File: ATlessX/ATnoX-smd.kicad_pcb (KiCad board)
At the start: 2 copper layers, 31 parts, among them J1 EXT_PWR_SW, J2 ATX, J3 P8, J4 P9, SW1 Power, U1 74LS74, U2 74LS14, U3 L7905

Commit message: Update PCB
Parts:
- moved J3 86.2 mm to (209.6, 129.5)
- moved J4 86.2 mm to (226.1, 129.5)
- moved C2 81.2 mm to (231.2, 115.0)
- moved C3 81.2 mm to (220.6, 113.7)
- moved R3 81.2 mm to (245.8, 109.2)
- moved R2 81.2 mm to (212.0, 117.2)
- moved R4 81.2 mm to (248.4, 103.9)
- moved R8 81.2 mm to (218.0, 117.2)
- moved C4 81.2 mm to (223.9, 117.0)
- moved D3 81.2 mm to (251.6, 107.3)
- moved D4 81.2 mm to (254.2, 101.6)
- moved D6 81.2 mm to (245.1, 112.5)
- moved D7 81.2 mm to (239.2, 116.1)
- moved R1 81.2 mm to (254.4, 98.3)
- moved R5 81.2 mm to (239.3, 112.7)
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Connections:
- D5 pad 2: (no net) -> /+12V
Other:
- board outline added: 80 x 47 mm

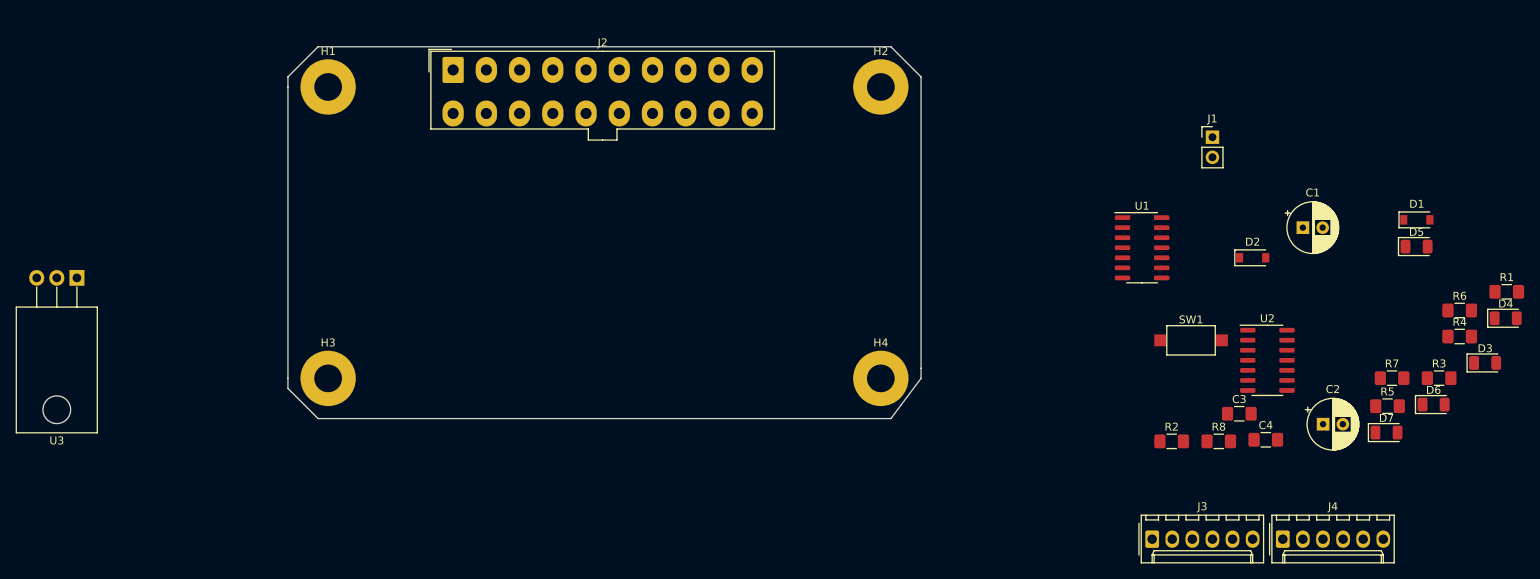
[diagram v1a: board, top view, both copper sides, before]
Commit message: Add SMD variant
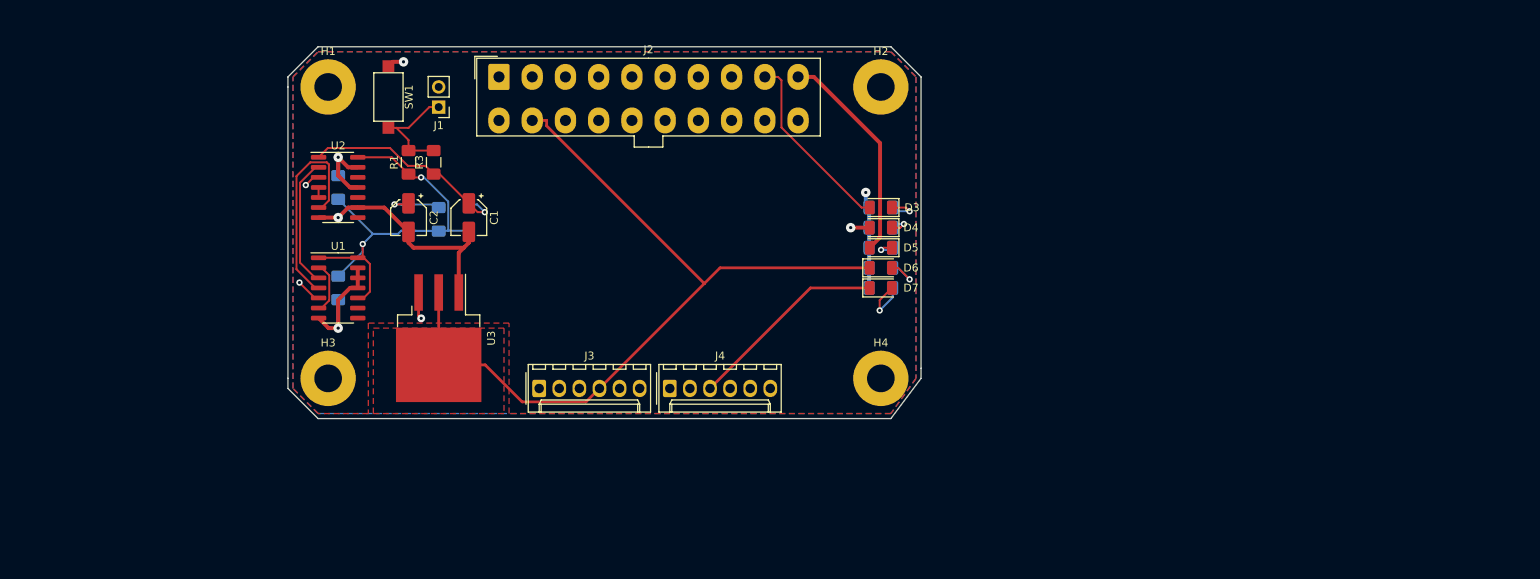
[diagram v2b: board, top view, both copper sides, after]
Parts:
- C1, C2: footprint Capacitor_THT:CP_Radial_D6.3mm_P2.50mm -> Capacitor_SMD:CP_Elec_4x5.3
- C3, C4, D1, D2, R2, R4, R5, R6, R7, R8: moved to B.Cu
- U3: footprint Package_TO_SOT_THT:TO-220-3_Horizontal_TabDown -> Package_TO_SOT_SMD:TO-263-3_TabPin2
- moved R1 139.8 mm to (115.6, 81.9), turned to 90 degrees
- moved R3 130.0 mm to (118.7, 81.9), turned to 90 degrees
- moved D1 119.8 mm to (123.2, 88.9), turned to 90 degrees
- moved U2 119.5 mm to (106.7, 85.1)
- moved C4 118.8 mm to (106.7, 97.8), turned to 270 degrees
- moved C2 118.5 mm to (115.6, 88.9), turned to 270 degrees
- moved C3 117.4 mm to (106.7, 85.1), turned to 90 degrees
- moved D2 106.8 mm to (115.6, 88.9), turned to 90 degrees
- moved SW1 106.0 mm to (113.0, 73.7), turned to 270 degrees
- moved C1 105.4 mm to (123.2, 88.9), turned to 270 degrees
- moved U1 101.7 mm to (106.7, 97.8)
- moved J1 97.9 mm to (119.4, 74.9), turned to 180 degrees
- moved R2 96.8 mm to (119.4, 89.1), turned to 90 degrees
- moved D4 79.8 mm to (175.3, 90.2), turned to 180 degrees
- moved J3 79.8 mm to (132.1, 110.5)
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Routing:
- net GND: track 0.00 -> 321.4 mm, vias 0 -> 5
- net /5VSB: track 0.00 -> 133.3 mm, vias 0 -> 2
- net VCC: track 0.00 -> 121.5 mm, vias 0 -> 1
- net /-12V: track 0.00 -> 103.3 mm
- net /+12V: track 0.00 -> 79.6 mm
- net /-5V: track 0.00 -> 70.4 mm, vias 0 -> 1
- net /PWR_OK: track 0.00 -> 50.4 mm
- net /~PS_ON: track 0.00 -> 49.8 mm, vias 0 -> 1
- net Net-(C1-Pad1): track 0.00 -> 27.3 mm, vias 0 -> 1
- net Net-(U1-Pad4): track 0.00 -> 26.7 mm
- net Net-(C2-Pad1): track 0.00 -> 21.8 mm, vias 0 -> 2
- net Net-(U1-Pad3): track 0.00 -> 16.4 mm
- net /PWR_SW: track 0.00 -> 14.1 mm
- net Net-(D7-Pad2): track 0.00 -> 7.01 mm, vias 0 -> 1
- net Net-(U1-Pad2): track 0.00 -> 6.65 mm
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- added copper zone on F.Cu, net /-12V
- added copper zone on B.Cu, net GND
- added copper zone on F.Cu, net GND
- added copper zone on In1.Cu, net GND
- added copper zone on In2.Cu, net VCC
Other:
- copper layers 2 -> 4

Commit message: Better ATnoX PCB
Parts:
- renumbered J3 to P8, J4 to P9
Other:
- board text added: "+12V"
- board text added: "+5V"
- board text added: "-12V"
- board text added: "-5V"
- board text added: "5VSB"
- board text added: "74HC14"
- board text added: "74HC74"
- board text added: "7905"
- board text added: "AT Power Connector"
- board text added: "ATX Power Connector"
- board text added: "ATnoX"
- board text added: "Design by"
- board text added: "Power Button"
- board text added: "SMD - Proto"
- board text added: "tabaglio@posteo.net"
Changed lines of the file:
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@@
   (general
     (thickness 1.6)
-    (drawings 11)
+    (drawings 26)
     (tracks 283)
     (zones 0)
@@
     (tags "D2PAK DDPAK TO-263 D2PAK-3 TO-263-3 SOT-404")
     (attr smd)
-    (fp_text reference U3 (at 0 -6.65 90) (layer F.SilkS)
+    (fp_text reference U3 (at -3.81 -5.08) (layer F.SilkS)
       (effects (font (size 1 1) (thickness 0.15)))
     )
@@
     (tags "SPST button tactile switch")
     (attr smd)
-    (fp_text reference SW1 (at 0 -2.6 90) (layer F.SilkS)
+    (fp_text reference SW1 (at 0 0 90) (layer F.SilkS)
       (effects (font (size 1 1) (thickness 0.15)))
     )
@@
     (tags "resistor handsolder")
     (attr smd)
-    (fp_text reference R6 (at 0 1.82) (layer B.SilkS)
+    (fp_text reference R6 (at -3.81 0) (layer B.SilkS)
       (effects (font (size 1 1) (thickness 0.15)) (justify mirror))
     )
@@
     (descr "Molex KK-254 Interconnect System, old/engineering part number: AE-6410-06A example for new part number: 22-27-2061, 6 Pins (http://www.molex.com/pdm_docs/sd/022272021_sd.pdf), generated with kicad-footprint-generator")
     (tags "connector Molex KK-254 side entry")
-    (fp_text reference J4 (at 6.35 -4.12) (layer F.SilkS)
+    (fp_text reference P9 (at 6.35 -4.12) (layer F.SilkS)
       (effects (font (size 1 1) (thickness 0.15)))
     )
@@
     (descr "Molex KK-254 Interconnect System, old/engineering part number: AE-6410-06A example for new part number: 22-27-2061, 6 Pins (http://www.molex.com/pdm_docs/sd/022272021_sd.pdf), generated with kicad-footprint-generator")
     (tags "connector Molex KK-254 side entry")
-    (fp_text reference J3 (at 6.35 -4.12) (layer F.SilkS)
+    (fp_text reference P8 (at 6.35 -4.12) (layer F.SilkS)
       (effects (font (size 1 1) (thickness 0.15)))
     )
@@
     (descr "Through hole straight pin header, 1x02, 2.54mm pitch, single row")
     (tags "Through hole pin header THT 1x02 2.54mm single row")
-    (fp_text reference J1 (at 0 -2.33) (layer F.SilkS)
+    (fp_text reference J1 (at -2.54 1.27 90) (layer F.SilkS)
       (effects (font (size 1 1) (thickness 0.15)))
     )
@@
     )
   )
+  (gr_text tabaglio@posteo.net (at 102.87 86.36 270) (layer B.SilkS)
+    (effects (font (size 1 1) (thickness 0.15) italic) (justify mirror))
+  )
+  (gr_text "Design by" (at 102.87 99.06 270) (layer B.SilkS)
+    (effects (font (size 1 1) (thickness 0.25)) (justify mirror))
+  )
+  (gr_text "SMD - Proto" (at 137.16 97.79) (layer F.SilkS)
+    (effects (font (size 1 1) (thickness 0.15) italic))
+  )
+  (gr_text ATnoX (at 146.05 93.98) (layer F.SilkS)
+    (effects (font (size 6 6) (thickness 0.5) italic))
+  )
+  (gr_text 7905 (at 113.03 100.33) (layer F.SilkS)
+    (effects (font (size 1 1) (thickness 0.15)))
+  )
+  (gr_text 74HC74 (at 106.68 97.79 90) (layer F.SilkS)
+    (effects (font (size 1 1) (thickness 0.15)))
+  )
+  (gr_text 74HC14 (at 106.68 85.09 90) (layer F.SilkS)
+    (effects (font (size 1 1) (thickness 0.15)))
+  )
+  (gr_text "Power Button" (at 116.84 73.66 90) (layer F.SilkS)
+    (effects (font (size 1 1) (thickness 0.15)))
+  )
+  (gr_text -5V (at 168.91 97.79) (layer F.SilkS)
+    (effects (font (size 1 1) (thickness 0.15)) (justify left))
+  )
+  (gr_text -12V (at 168.91 95.25) (layer F.SilkS)
+    (effects (font (size 1 1) (thickness 0.15)) (justify left))
+  )
+  (gr_text +12V (at 168.91 92.71) (layer F.SilkS)
+    (effects (font (size 1 1) (thickness 0.15)) (justify left))
+  )
+  (gr_text +5V (at 168.91 90.17) (layer F.SilkS)
+    (effects (font (size 1 1) (thickness 0.15)) (justify left))
+  )
+  (gr_text 5VSB (at 168.91 87.63) (layer F.SilkS)
+    (effects (font (size 1 1) (thickness 0.15)) (justify left))
+  )
+  (gr_text "ATX Power Connector" (at 146.05 81.28) (layer F.SilkS)
+    (effects (font (size 1 1) (thickness 0.15)))
+  )
+  (gr_text "AT  Power Connector" (at 146.05 104.14) (layer F.SilkS)
+    (effects (font (size 1 1) (thickness 0.15)))
+  )
   (gr_line (start 176.53 114.3) (end 180.34 109.22) (layer Edge.Cuts) (width 0.1))

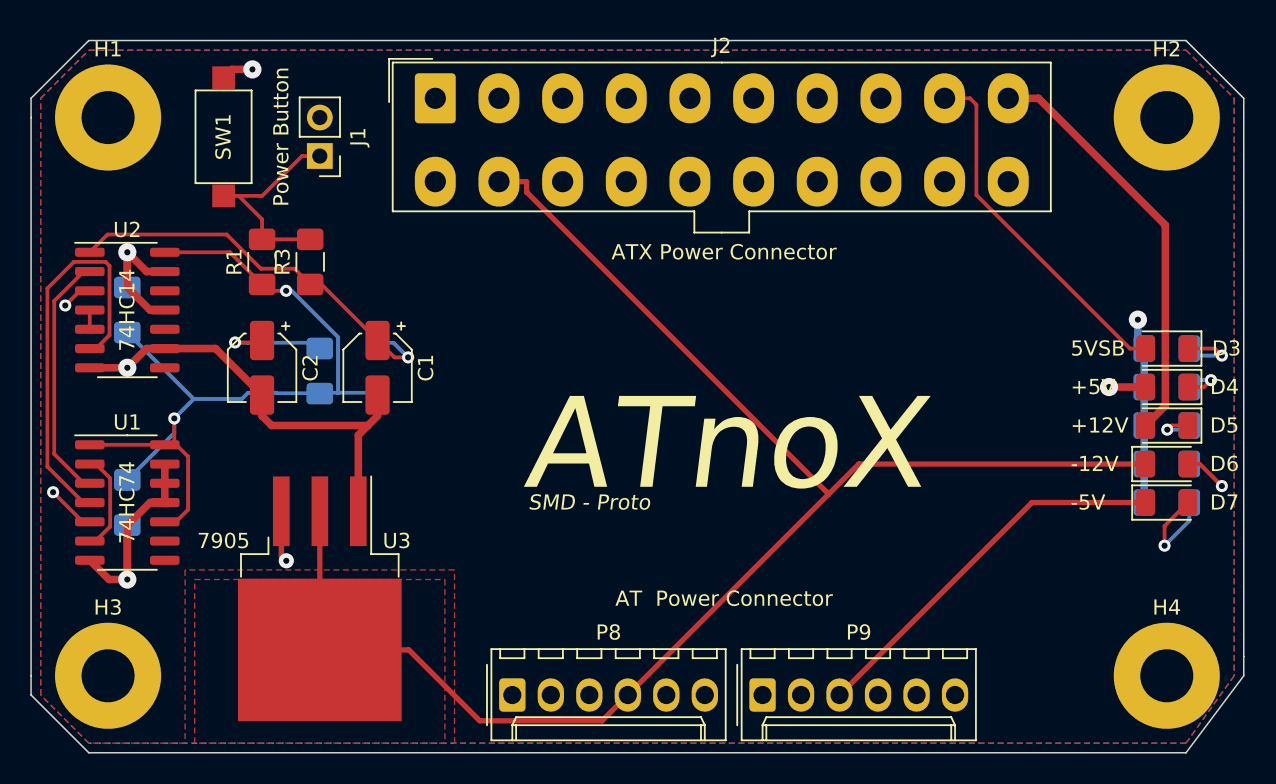
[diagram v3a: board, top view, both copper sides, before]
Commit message: Turned the SMD version into a 4layer board
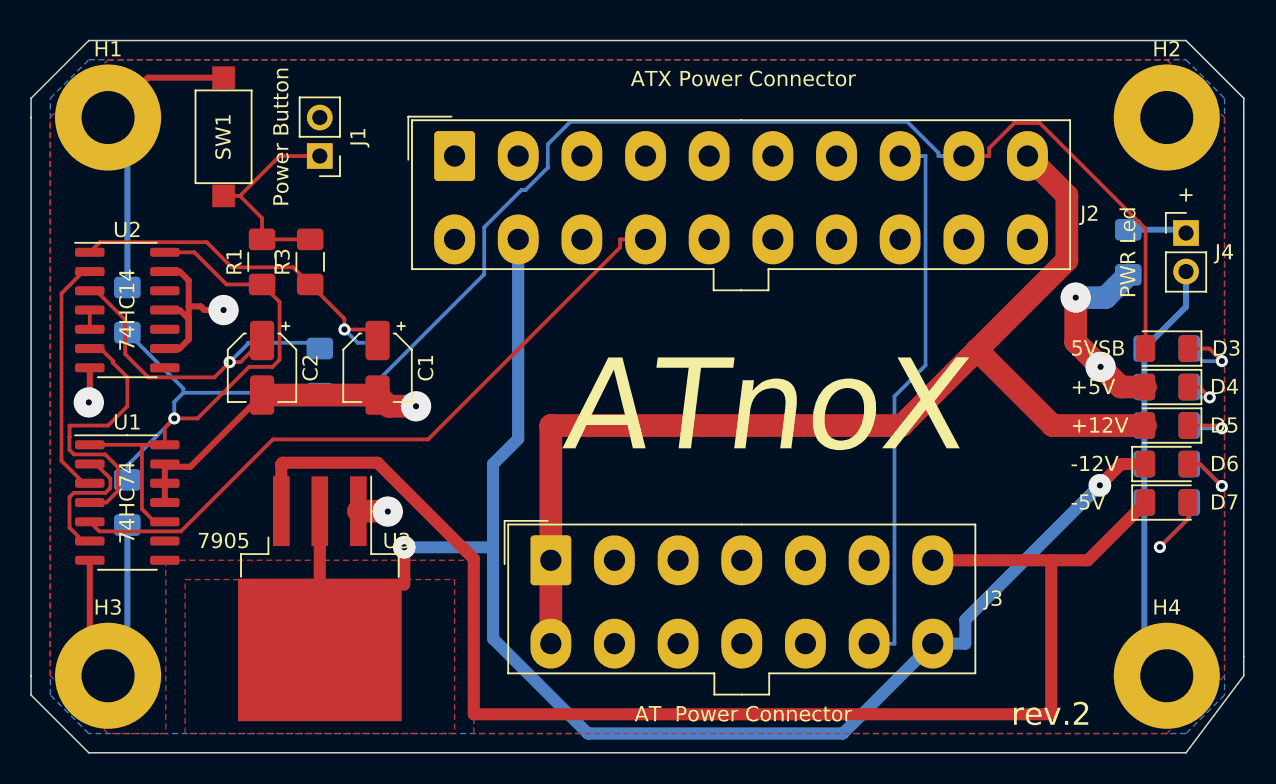
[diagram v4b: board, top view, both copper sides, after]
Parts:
- removed P8: P8, Connector_Molex:Molex_KK-254_AE-6410-06A_1x06_P2.54mm_Vertical
- removed P9: P9, Connector_Molex:Molex_KK-254_AE-6410-06A_1x06_P2.54mm_Vertical
- added J3: AT, Connector_Molex:Molex_Mini-Fit_Jr_5566-14A_2x07_P4.20mm_Vertical, F.Cu at (134.6, 101.6)
- added J4: PWR_LED, Connector_PinHeader_2.54mm:PinHeader_1x02_P2.54mm_Vertical, F.Cu at (176.5, 80.0)
- added R9: 1K, Resistor_SMD:R_1206_3216Metric_Pad1.42x1.75mm_HandSolder, B.Cu at (172.7, 81.3)
- moved J2 4.02 mm to (128.3, 74.9)
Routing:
- net GND: track 321.4 -> 389.8 mm, vias 5 -> 4
- net /-5V: track 70.4 -> 92.6 mm, vias 1 -> 0
- net /PWR_OK: track 50.4 -> 36.4 mm
- net Net-(U1-Pad4): track 26.7 -> 18.6 mm
- net VCC: track 121.5 -> 115.1 mm, vias 1 -> 2
- net /+12V: track 79.6 -> 74.1 mm
- net /~PS_ON: track 49.8 -> 45.2 mm, vias 1 -> 0
- net Net-(J4-Pad1): track 0.00 -> 3.90 mm
- net Net-(U1-Pad2): track 6.65 -> 9.03 mm
- net Net-(C1-Pad1): track 27.3 -> 24.9 mm
- net Net-(D5-Pad1): track 3.05 -> 4.53 mm
- net /-12V: track 103.3 -> 101.8 mm, vias 0 -> 2
- net /5VSB: track 133.3 -> 134.5 mm, vias 2 -> 1
- net Net-(C2-Pad1): track 21.8 -> 22.7 mm, vias 2 -> 1
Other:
- net class HiPower: trace_width 0.5 -> 1.5; via_dia 1.2 -> 2
- net class Power: clearance 0.3 -> 0.4; trace_width 0.35 -> 0.8; via_dia 1 -> 1.5
- board text added: "+"
- board text added: "PWR Led"
- board text added: "rev.2"
- board text removed: "SMD - Proto"

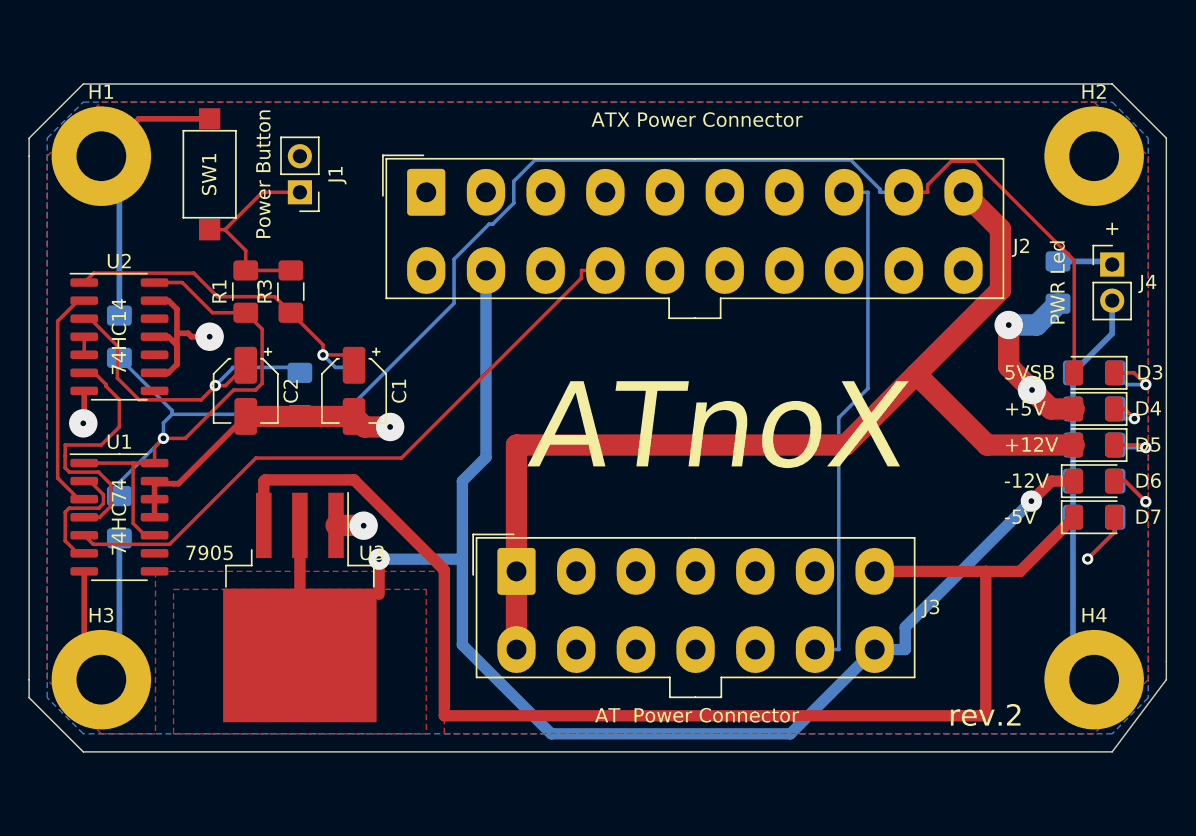
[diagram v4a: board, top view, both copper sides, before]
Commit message: Add rev. 2.5 of SMD variant
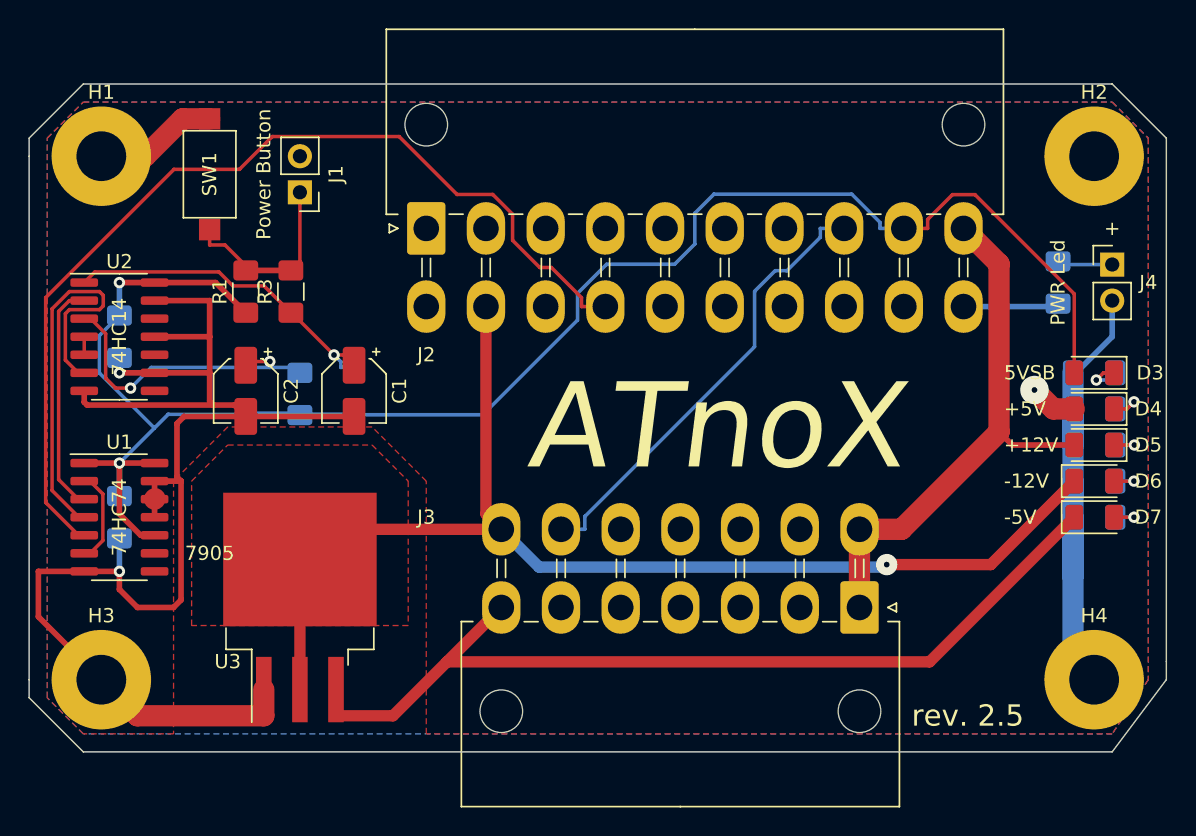
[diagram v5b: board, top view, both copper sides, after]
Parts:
- J2: footprint Connector_Molex:Molex_Mini-Fit_Jr_5566-20A_2x10_P4.20mm_Vertical -> Connector_Molex:Molex_Mini-Fit_Jr_5569-20A2_2x10_P4.20mm_Horizontal
- J3: footprint Connector_Molex:Molex_Mini-Fit_Jr_5566-14A_2x07_P4.20mm_Vertical -> Connector_Molex:Molex_Mini-Fit_Jr_5569-14A2_2x07_P4.20mm_Horizontal
- moved J3 24.3 mm to (158.8, 104.1), turned to 180 degrees
- moved J2 2.54 mm to (128.3, 77.5)
- turned C3 to 270 degrees
- turned U3 to 90 degrees
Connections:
- J2 pad 1: (no net) -> Net-(J2-Pad1)
- J2 pad 11: (no net) -> Net-(J2-Pad11)
- J2 pad 18: (no net) -> Net-(J2-Pad18)
- J2 pad 2: (no net) -> Net-(J2-Pad2)
- J3 pad 6: (no net) -> Net-(J3-Pad6)
- U1 pad 8: (no net) -> Net-(U1-Pad8)
- U1 pad 9: (no net) -> Net-(U1-Pad9)
- U2 pad 10: (no net) -> Net-(U2-Pad10)
- U2 pad 12: (no net) -> Net-(U2-Pad12)
- U2 pad 8: (no net) -> Net-(U2-Pad8)
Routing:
- net /+12V: track 74.1 -> 39.2 mm
- net /-5V: track 92.6 -> 65.0 mm
- net /~PS_ON: track 45.2 -> 68.5 mm
- net GND: track 389.8 -> 412.3 mm, vias 4 -> 2
- net /-12V: track 101.8 -> 81.7 mm, vias 2 -> 1
- net VCC: track 115.1 -> 104.0 mm, vias 2 -> 1
- net Net-(U1-Pad4): track 18.6 -> 28.6 mm
- net /5VSB: track 134.5 -> 124.7 mm, vias 1 -> 2
- net Net-(D7-Pad2): track 7.45 -> 2.73 mm
- net /PWR_OK: track 36.4 -> 31.9 mm
- net Net-(D6-Pad2): track 5.58 -> 2.72 mm
- net Net-(U1-Pad2): track 9.03 -> 6.65 mm
- net Net-(D3-Pad1): track 5.07 -> 3.00 mm
- net Net-(D5-Pad1): track 4.53 -> 2.78 mm
- net Net-(C1-Pad1): track 24.9 -> 24.0 mm
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- added copper zone on In2.Cu, net GND
- added copper zone on In1.Cu, net VCC
- removed copper zone on In1.Cu, net GND
- removed copper zone on In2.Cu, net VCC
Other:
- board text added: "rev. 2.5"
- board text removed: "rev.2"
